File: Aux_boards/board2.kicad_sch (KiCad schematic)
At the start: 7 parts, among them J2 Conn_01x04_Pin, U8 SFH6345, U9 SFH6345

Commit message: good version
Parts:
- added C1: 10uF, symbol Device:C
- added C3: 47uF, symbol Device:C
- added J1: Conn_01x04_Pin, symbol Connector:Conn_01x04_Pin
- added J1: DA15_Plug_MountingHoles, symbol Connector:DA15_Plug_MountingHoles
- added J3, J4, J5: Conn_01x03_Pin, symbol Connector:Conn_01x03_Pin
- added JP1, JP2: SolderJumper_3_Open, symbol Jumper:SolderJumper_3_Open
- added R1, R24, R4, R5, R7: 220R, symbol Device:R
- added R11, R19, R22, R23, R26, R27, R28, R3: 0R, symbol Device:R
- added R12, R13, R15, R16, R17, R18: 100k, symbol Device:R
- added R2, R21, R25, R6, R8, R9: 10R, symbol Device:R
- added U1: ~, power_modules:DSN-1504-3A, symbol power_modules:DSN-1504-3A
- added U2: AMS1117-3.3, Package_TO_SOT_SMD:SOT-223-3_TabPin2, symbol Regulator_Linear:AMS1117-3.3
- added U3, U4, U5, U6, U7: SFH6345, SFH6345:DIP762W50P254L977H451Q8, symbol SFH6345:SFH6345
- renumbered R8 to R20
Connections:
- net GND: now also C2.2, U8.5, U9.5, C1.1, C3.2, J1.0 (PAD), J1.10 (P10), J1.12 (P12), J1.14 (P14), J1.2, J1.4, J1.4 (Pin_4), J1.6, J3.3 (Pin_3), J4.3 (Pin_3), J5.3 (Pin_3), R11.2, R19.2, R22.2, R23.2, R26.2, R27.2, R3.2, U1.3 (Vin-), U1.4 (Vin-), U1.5 (Vout-), U1.6 (Vout-), U2.1 (GND), U3.5, U4.5, U5.5, U6.5, U7.5
- net R_ENC_A: now also U5.2
- net R_ENC_A_24: now also J1.3, R16.2, U5.6
- net R_ENC_B: now also U6.2
- net R_ENC_B_24: now also J1.11 (P111), U6.6
- net Z_ENC_A: now also J1.2 (Pin_2), U3.2
- net Z_ENC_A_24: now also J1.1, R12.2, U3.6
- net Z_ENC_B: now also J1.3 (Pin_3), R13.2, U4.2, U4.6
- net Z_ENC_B_24: now also J1.9 (P9)
- net Z_LIM_DN: now also J3.2 (Pin_2)
- net Z_LIM_DN_24: now also J1.13 (P13), R18.2
- net Z_LIM_UP: now also J4.2 (Pin_2), U7.2
- net Z_LIM_UP_24: now also J1.5, R15.2, U7.6
- net Z_POS: now also J5.2 (Pin_2)
- net Z_Pos_24: now also J1.7, R17.2
- net at R20.1: now also U7.3
- net at R20.2: now also R21.1
- net at J2.1 (Pin_1): now also JP2.2 (C)
- net +3.3V: now reaches C2.1
- net +3.3V: now also J5.1 (Pin_1), U2.2 (VO)
- net at R10.2: now also R28.1
- net +24V: now reaches R14.1
- net +24V: now also U8.8, U9.8, J1.15 (P15), J1.8, JP1.1 (A), JP2.1 (A), R12.1, R13.1, R15.1, R16.1, R17.1, R18.1, U1.1 (Vin+), U1.2 (Vin+), U3.8, U4.8, U5.8, U6.8, U7.8
- net at U8.3: now also R4.1
- new net: R5.1, U4.3
- new net: R5.2, R6.1
- new net: R7.1, U5.3
- new net: R7.2, R8.1
- new net: R22.1, R8.2
- new net: R11.1, R6.2
- new net: R1.2, R2.1
- new net: R2.2, R3.1
- new net: R4.2, R9.1
- new net: J1.1 (Pin_1), JP1.2 (C)
- new net: R24.1, U3.3
- new net: R21.2, R23.1
- new net: R1.1, U6.3
- new net: R27.1, R28.2
- new net: R24.2, R25.1
- new net: R25.2, R26.1
- new net: R19.1, R9.2
- new net +5V: C1.2, C3.1, J3.1 (Pin_1), J4.1 (Pin_1), JP1.3 (B), JP2.3 (B), U1.7 (Vout+), U1.8 (Vout+), U2.3 (VI)

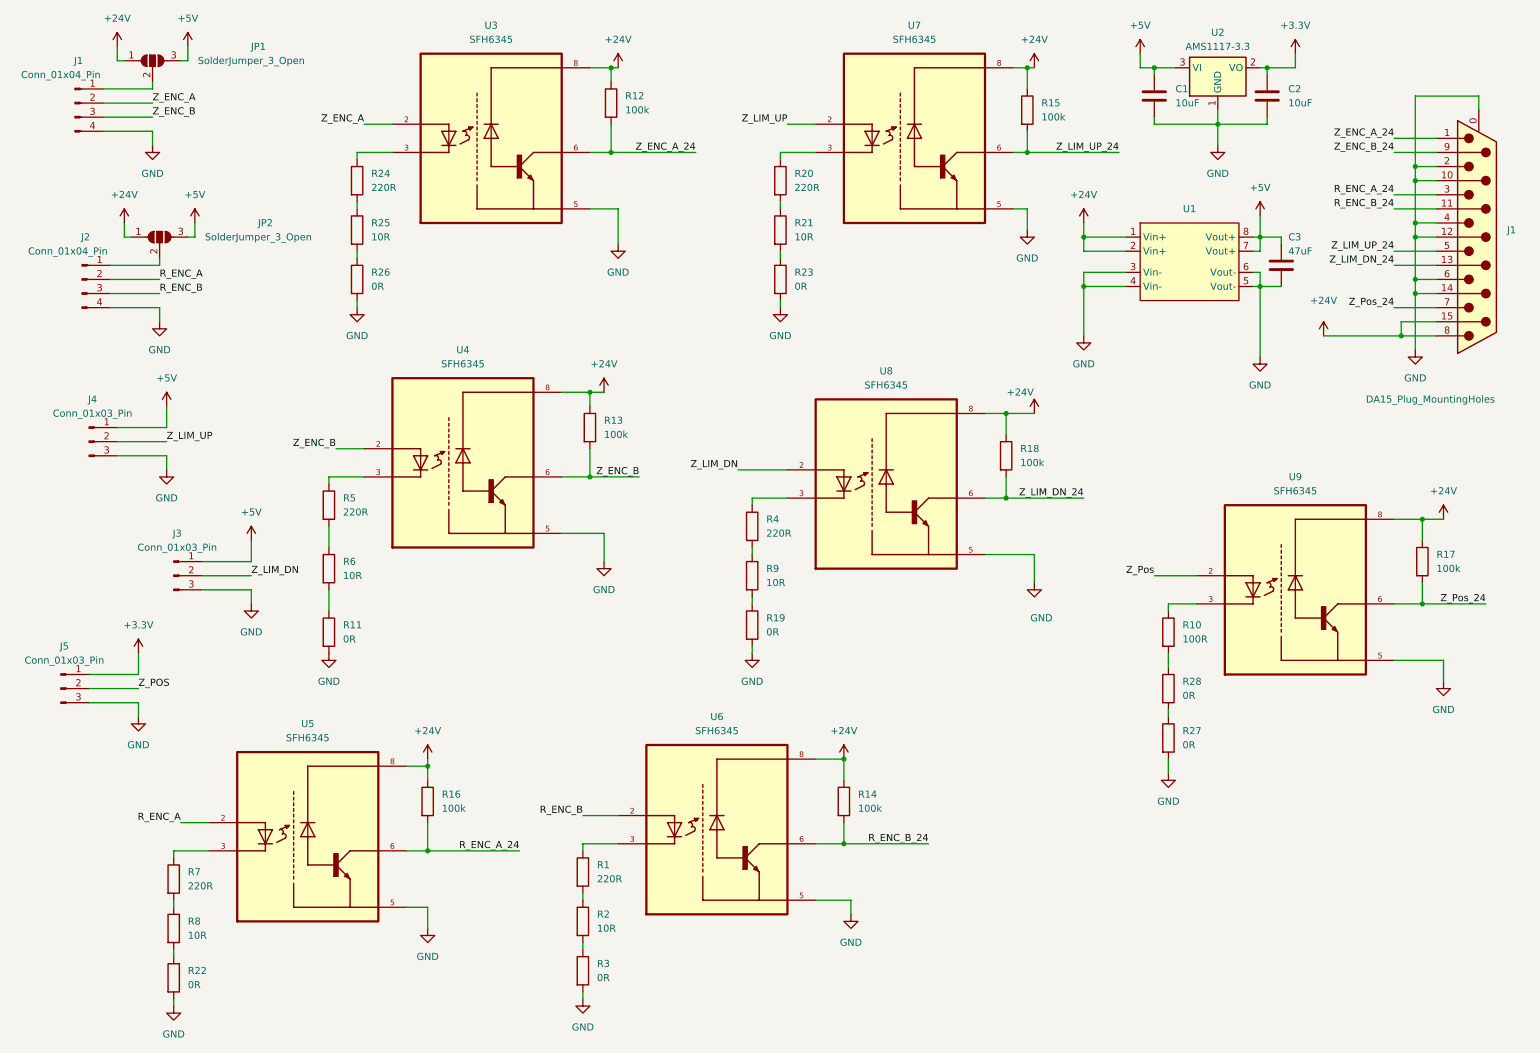
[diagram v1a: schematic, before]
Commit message: Removed unnecessary optocouplers
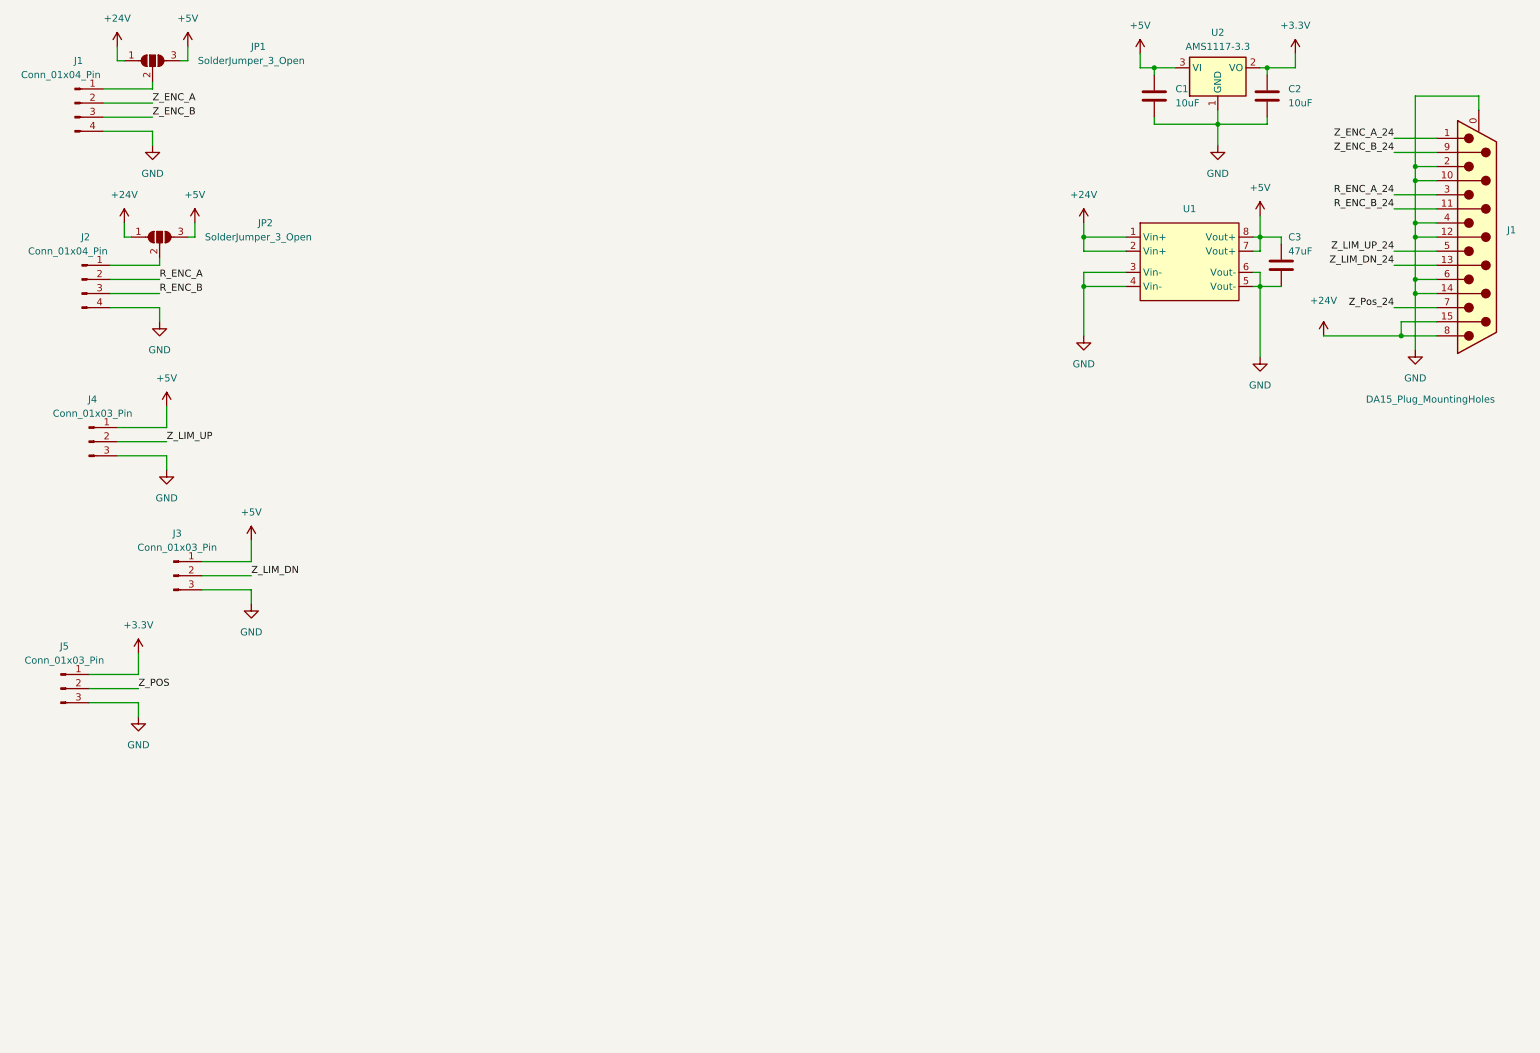
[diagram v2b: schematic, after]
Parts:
- removed R1, R20, R24, R4, R5, R7: 220R, symbol Device:R
- removed R10: 100R, symbol Device:R
- removed R11, R19, R22, R23, R26, R27, R28, R3: 0R, symbol Device:R
- removed R12, R13, R14, R15, R16, R17, R18: 100k, symbol Device:R
- removed R2, R21, R25, R6, R8, R9: 10R, symbol Device:R
- removed U3, U4, U5, U6, U7, U8, U9: SFH6345, SFH6345:DIP762W50P254L977H451Q8, symbol SFH6345:SFH6345
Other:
- title: Karcsi (INDACT Robot Arm) - Aux. control board II. -> Karcsi (INDACT Robot Arm) - Auxiliary board 2
